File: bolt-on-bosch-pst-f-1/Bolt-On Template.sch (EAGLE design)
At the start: 10 parts

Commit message: cleanup board design
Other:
- moved on the sheet: D1, R_PRESS_BOT
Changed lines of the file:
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@@
 <attribute name="VALUE" x="254" y="133.35" size="1.778" layer="96"/>
 </instance>
-<instance part="D1" gate="G$1" x="180.34" y="60.96" smashed="yes">
-<attribute name="NAME" x="178.054" y="62.865" size="1.778" layer="95"/>
-<attribute name="VALUE" x="178.054" y="57.531" size="1.778" layer="96"/>
+<instance part="D1" gate="G$1" x="198.12" y="66.04" smashed="yes">
+<attribute name="NAME" x="195.834" y="67.945" size="1.778" layer="95"/>
+<attribute name="VALUE" x="195.834" y="62.611" size="1.778" layer="96"/>
 </instance>
 <instance part="R_TEMP_TOP" gate="G$1" x="248.92" y="83.82" smashed="yes" rot="R90">
@@
 <attribute name="VALUE" x="171.45" y="67.818" size="1.778" layer="96"/>
 </instance>
-<instance part="R_PRESS_BOT" gate="G$1" x="193.04" y="66.04" smashed="yes">
-<attribute name="NAME" x="189.23" y="67.5386" size="1.778" layer="95"/>
-<attribute name="VALUE" x="189.23" y="62.738" size="1.778" layer="96"/>
+<instance part="R_PRESS_BOT" gate="G$1" x="175.26" y="60.96" smashed="yes">
+<attribute name="NAME" x="171.45" y="62.4586" size="1.778" layer="95"/>
+<attribute name="VALUE" x="171.45" y="57.658" size="1.778" layer="96"/>
 </instance>
 <instance part="C2" gate="G$1" x="233.68" y="86.36" smashed="yes">
@@
 <junction x="213.36" y="143.51"/>
 <wire x1="233.68" y1="88.9" x2="233.68" y2="96.52" width="0.1524" layer="91"/>
-<wire x1="266.7" y1="143.51" x2="213.36" y2="143.51" width="0.1524" layer="91"/>
-<wire x1="261.62" y1="66.04" x2="261.62" y2="96.52" width="0.1524" layer="91"/>
+<wire x1="261.62" y1="60.96" x2="261.62" y2="96.52" width="0.1524" layer="91"/>
 <junction x="261.62" y="96.52"/>
-<wire x1="198.12" y1="66.04" x2="261.62" y2="66.04" width="0.1524" layer="91"/>
+<wire x1="180.34" y1="60.96" x2="261.62" y2="60.96" width="0.1524" layer="91"/>
 <pinref part="R_PRESS_BOT" gate="G$1" pin="2"/>
-<wire x1="266.7" y1="66.04" x2="266.7" y2="143.51" width="0.1524" layer="91"/>
+<wire x1="266.7" y1="66.04" x2="266.7" y2="96.52" width="0.1524" layer="91"/>
 <pinref part="C1" gate="G$1" pin="1"/>
 <pinref part="C2" gate="G$1" pin="1"/>
@@
 <wire x1="233.68" y1="96.52" x2="205.74" y2="96.52" width="0.1524" layer="91"/>
 <junction x="233.68" y="96.52"/>
+<wire x1="261.62" y1="96.52" x2="266.7" y2="96.52" width="0.1524" layer="91"/>
 </segment>
 </net>
@@
 <junction x="213.36" y="133.35"/>
 <pinref part="D1" gate="G$1" pin="C"/>
-<wire x1="182.88" y1="60.96" x2="264.16" y2="60.96" width="0.1524" layer="91"/>
-<wire x1="264.16" y1="60.96" x2="264.16" y2="129.54" width="0.1524" layer="91"/>
-<wire x1="264.16" y1="129.54" x2="251.46" y2="129.54" width="0.1524" layer="91"/>
+<wire x1="200.66" y1="66.04" x2="254" y2="66.04" width="0.1524" layer="91"/>
+<wire x1="254" y1="66.04" x2="254" y2="129.54" width="0.1524" layer="91"/>
+<wire x1="254" y1="129.54" x2="251.46" y2="129.54" width="0.1524" layer="91"/>
 <wire x1="251.46" y1="129.54" x2="251.46" y2="135.89" width="0.1524" layer="91"/>
 <wire x1="251.46" y1="135.89" x2="213.36" y2="135.89" width="0.1524" layer="91"/>
@@
 <wire x1="147.32" y1="71.12" x2="147.32" y2="66.04" width="0.1524" layer="91"/>
 <wire x1="147.32" y1="66.04" x2="147.32" y2="60.96" width="0.1524" layer="91"/>
-<wire x1="147.32" y1="60.96" x2="177.8" y2="60.96" width="0.1524" layer="91"/>
-<wire x1="187.96" y1="66.04" x2="147.32" y2="66.04" width="0.1524" layer="91"/>
-<junction x="147.32" y="66.04"/>
+<wire x1="147.32" y1="66.04" x2="195.58" y2="66.04" width="0.1524" layer="91"/>
+<wire x1="170.18" y1="60.96" x2="147.32" y2="60.96" width="0.1524" layer="91"/>
+<junction x="147.32" y="60.96"/>
 <wire x1="170.18" y1="71.12" x2="147.32" y2="71.12" width="0.1524" layer="91"/>
 <pinref part="R_PRESS_TOP" gate="G$1" pin="1"/>
@@
 <wire x1="266.7" y1="58.42" x2="266.7" y2="55.88" width="0.1524" layer="91"/>
 <wire x1="266.7" y1="55.88" x2="147.32" y2="55.88" width="0.1524" layer="91"/>
-<wire x1="147.32" y1="55.88" x2="147.32" y2="60.96" width="0.1524" layer="91"/>
-<junction x="147.32" y="60.96"/>
+<junction x="147.32" y="66.04"/>
+<wire x1="147.32" y1="60.96" x2="147.32" y2="55.88" width="0.1524" layer="91"/>
 </segment>
 </net>
@@
 <wire x1="210.82" y1="88.9" x2="210.82" y2="81.28" width="0.1524" layer="91"/>
 <wire x1="210.82" y1="81.28" x2="195.58" y2="81.28" width="0.1524" layer="91"/>
-<wire x1="195.58" y1="81.28" x2="195.58" y2="160.02" width="0.1524" layer="91"/>
-<wire x1="195.58" y1="160.02" x2="251.46" y2="160.02" width="0.1524" layer="91"/>
+<wire x1="195.58" y1="81.28" x2="195.58" y2="162.56" width="0.1524" layer="91"/>
 <wire x1="229.87" y1="138.43" x2="238.76" y2="138.43" width="0.1524" layer="91"/>
 <pinref part="SV2" gate="1" pin="15"/>
@@
 <wire x1="254" y1="140.97" x2="213.36" y2="140.97" width="0.1524" layer="91"/>
 <junction x="213.36" y="138.43"/>
-<wire x1="251.46" y1="160.02" x2="251.46" y2="140.97" width="0.1524" layer="91"/>
-<wire x1="251.46" y1="140.97" x2="213.36" y2="140.97" width="0.1524" layer="91"/>
 <junction x="213.36" y="140.97"/>
 <pinref part="CAN_X2_5V" gate="G$1" pin="1"/>
-<wire x1="254" y1="162.56" x2="147.32" y2="162.56" width="0.1524" layer="91"/>
+<wire x1="254" y1="162.56" x2="195.58" y2="162.56" width="0.1524" layer="91"/>
 <pinref part="PST-F_1_IN" gate="G$1" pin="1"/>
+<wire x1="195.58" y1="162.56" x2="147.32" y2="162.56" width="0.1524" layer="91"/>
 <wire x1="210.82" y1="88.9" x2="205.74" y2="88.9" width="0.1524" layer="91"/>
-</segment>
-</net>
+<junction x="195.58" y="162.56"/>
+</segment>
+</net>

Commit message: cleanup board design
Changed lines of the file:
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@@
 <wire x1="210.82" y1="88.9" x2="210.82" y2="81.28" width="0.1524" layer="91"/>
 <wire x1="210.82" y1="81.28" x2="195.58" y2="81.28" width="0.1524" layer="91"/>
-<wire x1="195.58" y1="81.28" x2="195.58" y2="162.56" width="0.1524" layer="91"/>
+<wire x1="195.58" y1="81.28" x2="195.58" y2="160.02" width="0.1524" layer="91"/>
 <wire x1="229.87" y1="138.43" x2="238.76" y2="138.43" width="0.1524" layer="91"/>
 <pinref part="SV2" gate="1" pin="15"/>
@@
 <wire x1="213.36" y1="138.43" x2="229.87" y2="138.43" width="0.1524" layer="91"/>
 <label x="238.76" y="138.43" size="1.27" layer="95" xref="yes"/>
-<wire x1="254" y1="162.56" x2="254" y2="140.97" width="0.1524" layer="91"/>
-<wire x1="254" y1="140.97" x2="213.36" y2="140.97" width="0.1524" layer="91"/>
 <junction x="213.36" y="138.43"/>
+<pinref part="CAN_X2_5V" gate="G$1" pin="1"/>
+<wire x1="254" y1="162.56" x2="147.32" y2="162.56" width="0.1524" layer="91"/>
+<pinref part="PST-F_1_IN" gate="G$1" pin="1"/>
+<wire x1="210.82" y1="88.9" x2="205.74" y2="88.9" width="0.1524" layer="91"/>
+<wire x1="254" y1="162.56" x2="254" y2="138.43" width="0.1524" layer="91"/>
+<wire x1="254" y1="138.43" x2="213.36" y2="138.43" width="0.1524" layer="91"/>
+<wire x1="195.58" y1="160.02" x2="251.46" y2="160.02" width="0.1524" layer="91"/>
+<wire x1="251.46" y1="160.02" x2="251.46" y2="140.97" width="0.1524" layer="91"/>
+<wire x1="251.46" y1="140.97" x2="213.36" y2="140.97" width="0.1524" layer="91"/>
 <junction x="213.36" y="140.97"/>
-<pinref part="CAN_X2_5V" gate="G$1" pin="1"/>
-<wire x1="254" y1="162.56" x2="195.58" y2="162.56" width="0.1524" layer="91"/>
-<pinref part="PST-F_1_IN" gate="G$1" pin="1"/>
-<wire x1="195.58" y1="162.56" x2="147.32" y2="162.56" width="0.1524" layer="91"/>
-<wire x1="210.82" y1="88.9" x2="205.74" y2="88.9" width="0.1524" layer="91"/>
-<junction x="195.58" y="162.56"/>
 </segment>
 </net>

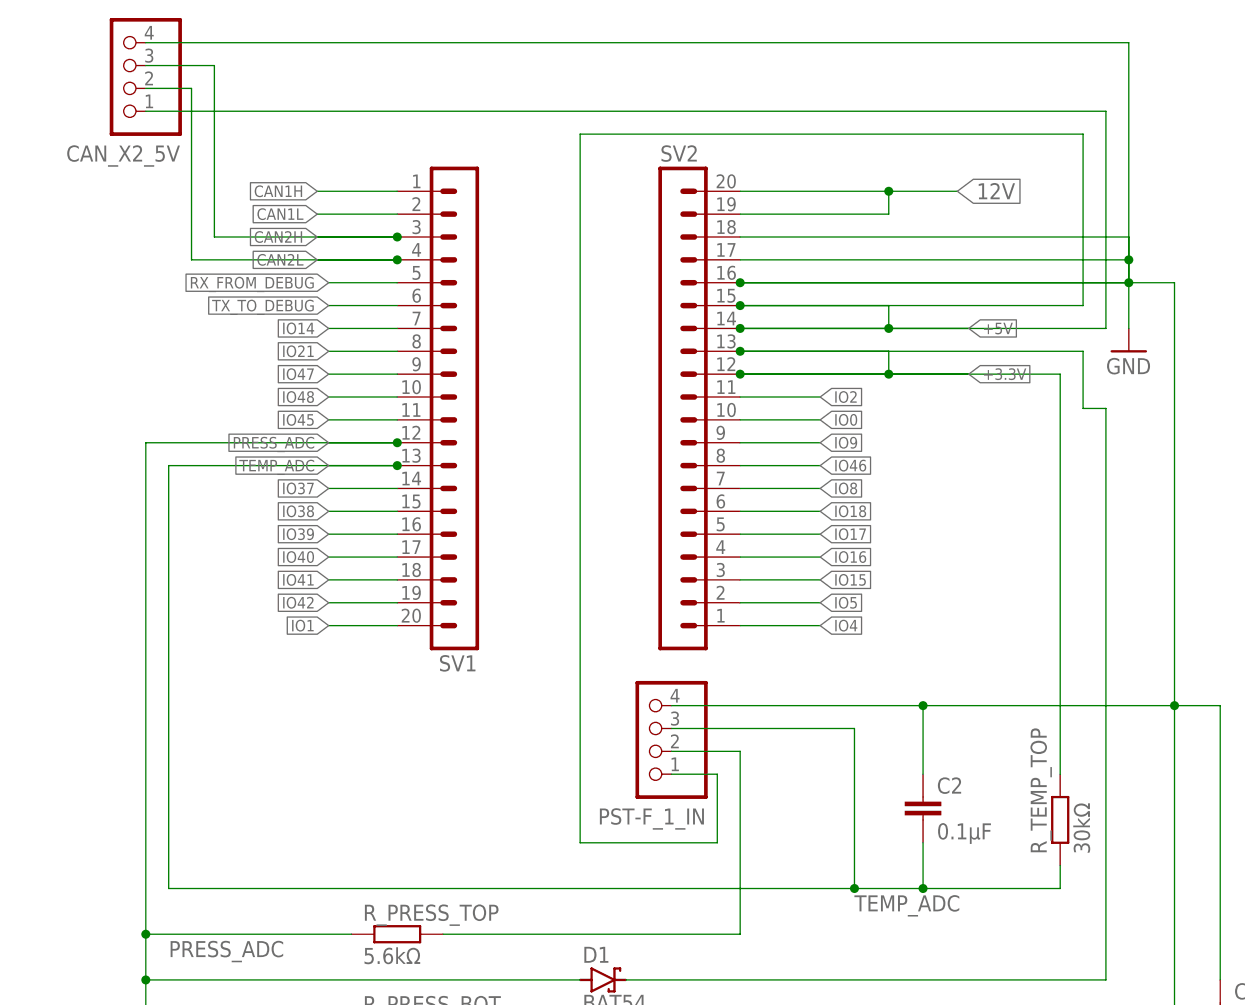
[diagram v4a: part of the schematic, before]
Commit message: add labels to jst pins
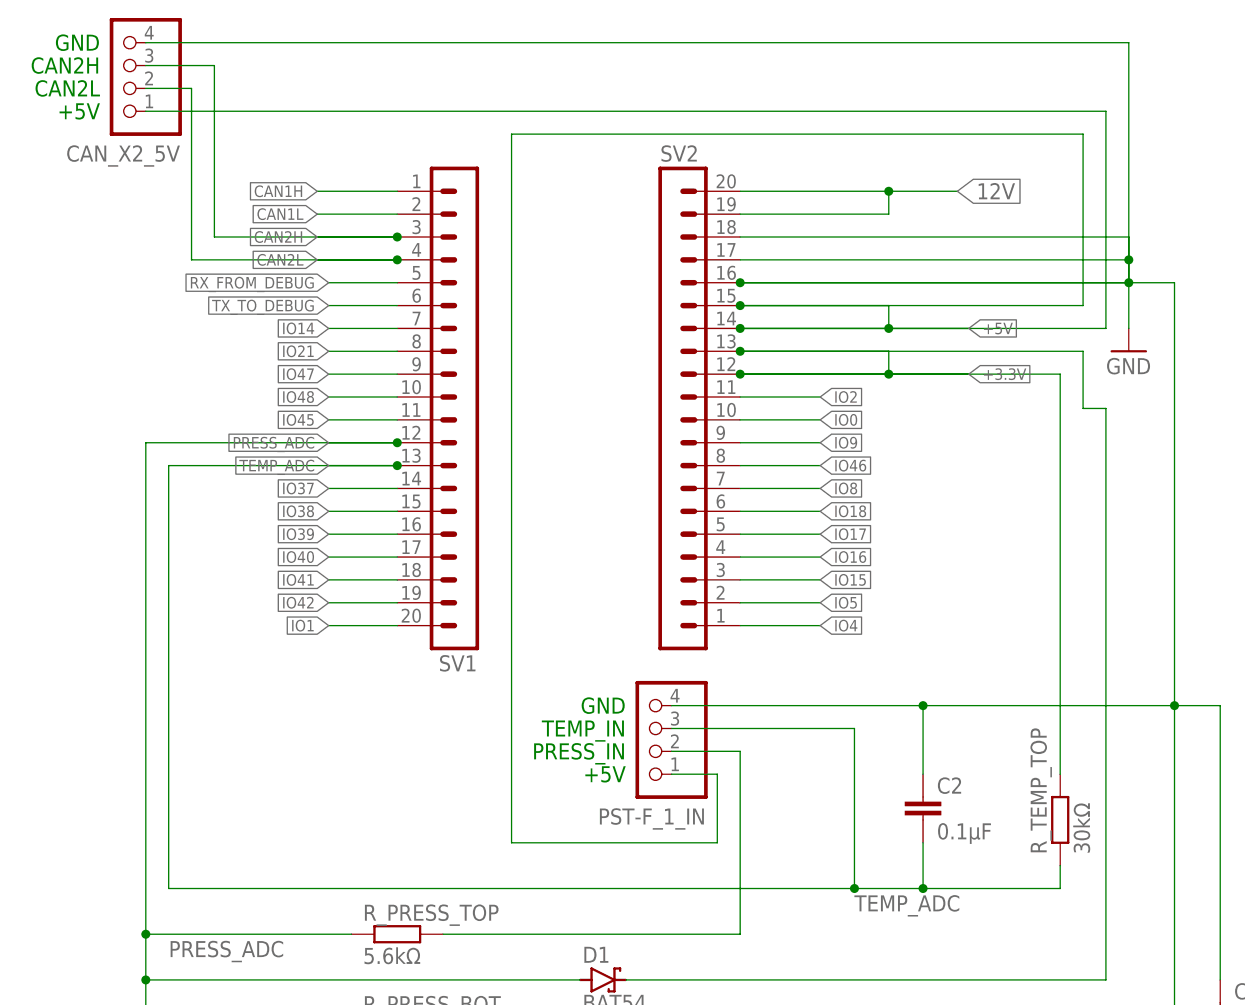
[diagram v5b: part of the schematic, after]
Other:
- note added: "+5V"
- note added: "CAN2H"
- note added: "CAN2L"
- note added: "GND"
- note added: "PRESS_IN"
- note added: "TEMP_IN"
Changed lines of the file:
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@@
 <plain>
 <text x="345.44" y="20.32" size="1.778" layer="97">IO/Sensors</text>
+<text x="142.24" y="170.18" size="1.778" layer="91" align="center-right">GND</text>
+<text x="142.24" y="167.64" size="1.778" layer="91" align="center-right">CAN2H</text>
+<text x="142.24" y="165.1" size="1.778" layer="91" align="center-right">CAN2L</text>
+<text x="142.24" y="162.56" size="1.778" layer="91" align="center-right">+5V</text>
+<text x="200.66" y="96.52" size="1.778" layer="91" align="center-right">GND</text>
+<text x="200.66" y="93.98" size="1.778" layer="91" align="center-right">TEMP_IN</text>
+<text x="200.66" y="91.44" size="1.778" layer="91" align="center-right">PRESS_IN</text>
+<text x="200.66" y="88.9" size="1.778" layer="91" align="center-right">+5V</text>
 </plain>
 <instances>
@@
 <segment>
 <wire x1="210.82" y1="88.9" x2="210.82" y2="81.28" width="0.1524" layer="91"/>
-<wire x1="210.82" y1="81.28" x2="195.58" y2="81.28" width="0.1524" layer="91"/>
-<wire x1="195.58" y1="81.28" x2="195.58" y2="160.02" width="0.1524" layer="91"/>
+<wire x1="210.82" y1="81.28" x2="187.96" y2="81.28" width="0.1524" layer="91"/>
+<wire x1="187.96" y1="81.28" x2="187.96" y2="160.02" width="0.1524" layer="91"/>
 <wire x1="229.87" y1="138.43" x2="238.76" y2="138.43" width="0.1524" layer="91"/>
 <pinref part="SV2" gate="1" pin="15"/>
@@
 <wire x1="254" y1="162.56" x2="254" y2="138.43" width="0.1524" layer="91"/>
 <wire x1="254" y1="138.43" x2="213.36" y2="138.43" width="0.1524" layer="91"/>
-<wire x1="195.58" y1="160.02" x2="251.46" y2="160.02" width="0.1524" layer="91"/>
+<wire x1="187.96" y1="160.02" x2="251.46" y2="160.02" width="0.1524" layer="91"/>
 <wire x1="251.46" y1="160.02" x2="251.46" y2="140.97" width="0.1524" layer="91"/>
 <wire x1="251.46" y1="140.97" x2="213.36" y2="140.97" width="0.1524" layer="91"/>
